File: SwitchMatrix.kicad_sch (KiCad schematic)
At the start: 0 parts

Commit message: Some matrix stuff
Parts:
- added D1, D? (x14): 1N4148, symbol Device:D_Small
- added SW1, SW? (x13): 1u, marbastlib-mx:SW_MX_1u, symbol marbastlib-mx:MX_SW_solder
- added SW?: 2u, marbastlib-mx:SW_MX_1u, symbol marbastlib-mx:MX_SW_solder
- added SW?: RotaryEncoder_Switch, symbol Device:RotaryEncoder_Switch

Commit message: Some stuff
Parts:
- removed D?: 1N4148, symbol Device:D_Small
- removed SW?: 2u, marbastlib-mx:SW_MX_1u, symbol marbastlib-mx:MX_SW_solder
- added D15, D16, D18, D20, D21, D22, D23, D24, D25, D26, D27, D28, D29, D30: 1N4148, symbol Device:D_Small
- added SW? (x13): 1u, marbastlib-mx:SW_MX_1u, symbol marbastlib-mx:MX_SW_solder
- added SW?: 1.5u, marbastlib-mx:SW_MX_1u, symbol marbastlib-mx:MX_SW_solder
- SW14: renamed from SW?; value 1u -> 2u
- gave numbers to parts that had none: 25
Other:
- moved on the sheet: SW?

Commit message: Some matrix work
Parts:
- removed D1, D10, D11, D12, D13, D14, D15, D16, D18, D2, D20, D21, D22, D23, D24, D25, D26, D27, D28, D29, D3, D30, D4, D5, D6, D7, D8, D9: 1N4148, symbol Device:D_Small
- removed SW1, SW10, SW11, SW12, SW13, SW2, SW3, SW4, SW5, SW6, SW7, SW8, SW9, SW? (x13): 1u, marbastlib-mx:SW_MX_1u, symbol marbastlib-mx:MX_SW_solder
- removed SW14: 2u, marbastlib-mx:SW_MX_1u, symbol marbastlib-mx:MX_SW_solder
- removed SW?: 1.5u, marbastlib-mx:SW_MX_1u, symbol marbastlib-mx:MX_SW_solder
- removed SW?: RotaryEncoder_Switch, symbol Device:RotaryEncoder_Switch
- added D? (x31): 1N4148, symbol Device:D_Small
- added SW? (x30): 1u, marbastlib-mx:SW_MX_1u, symbol marbastlib-mx:MX_SW_solder
- added SW?: 2u, marbastlib-mx:SW_MX_1u, symbol marbastlib-mx:MX_SW_solder
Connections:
- new net: D?.2 (A), SW?.2 (x31)

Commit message: Some more matrix stuff
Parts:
- removed D?: 1N4148, symbol Device:D_Small
- added D? (x41): 1N4148, symbol Device:D_Small
- added SW? (x34): 1u, marbastlib-mx:SW_MX_1u, symbol marbastlib-mx:MX_SW_solder
- added SW?: 7u, marbastlib-mx:SW_MX_1u, symbol marbastlib-mx:MX_SW_solder
- added SW?: 1.75u, marbastlib-mx:SW_MX_1u, symbol marbastlib-mx:MX_SW_solder
- added SW?: 2.25u, marbastlib-mx:SW_MX_1u, symbol marbastlib-mx:MX_SW_solder
- added SW? (x2): 1.5u, marbastlib-mx:SW_MX_1u, symbol marbastlib-mx:MX_SW_solder
- added SW? (x2): 1.25u, marbastlib-mx:SW_MX_1u, symbol marbastlib-mx:MX_SW_solder
- SW?: value 1u -> 1.5u
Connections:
- net COL0: now reaches SW?.1
- net COL0: now also SW?.1, SW?.1, SW?.1, SW?.1, SW?.1
- new net: D?.2 (A), SW?.2 (x41)
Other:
- moved on the sheet: D?, SW?

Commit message: Columns
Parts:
- removed D?: 1N4148, symbol Device:D_Small
- added SW? (x5): 1.25u, marbastlib-mx:SW_MX_1u, symbol marbastlib-mx:MX_SW_solder
- added SW?: 6.25u, marbastlib-mx:SW_MX_1u, symbol marbastlib-mx:MX_SW_solder
- SW?: value 1u -> 1.5u
- gave numbers to parts that had none: 6
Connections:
- net COL4: now reaches SW?.1
- net COL4: now also SW5.1, SW?.1, SW?.1
- net COL8: now reaches SW?.1
- net COL8: now also SW?.1, SW?.1, SW?.1
- net COL9: now reaches SW?.1
- net COL9: now also SW?.1, SW?.1, SW?.1, SW?.1
- net COL6: now reaches SW?.1
- net COL6: now also SW?.1, SW?.1, SW?.1, SW?.1, SW?.1
- net COL13: now reaches SW?.1
- net COL13: now also SW?.1, SW?.1, SW?.1, SW?.1
- net COL15: now reaches SW?.1
- net COL15: now also SW?.1, SW?.1, SW?.1, SW?.1
- net COL12: now reaches SW?.1
- net COL12: now also SW?.1, SW?.1, SW?.1, SW?.1
- net COL3: now reaches SW?.1
- net COL3: now also SW4.1, SW?.1, SW?.1
- net COL10: now reaches SW?.1
- net COL10: now also SW?.1, SW?.1, SW?.1
- net COL1: now reaches SW?.1
- net COL1: now also SW2.1, SW?.1, SW?.1, SW?.1, SW?.1
- net COL11: now reaches SW?.1
- net COL11: now also SW?.1, SW?.1, SW?.1, SW?.1, SW?.1
- net COL5: now reaches SW?.1
- net COL5: now also SW6.1, SW?.1, SW?.1
- net COL14: now reaches SW?.1
- net COL14: now also SW?.1
- net at D?.2 (A), SW?.2: now also SW?.2
- net COL2: now reaches SW?.1
- net COL2: now also SW3.1, SW?.1, SW?.1, SW?.1, SW?.1
- net COL7: now reaches SW?.1
- net COL7: now also SW?.1, SW?.1, SW?.1
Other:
- moved on the sheet: D?, SW?

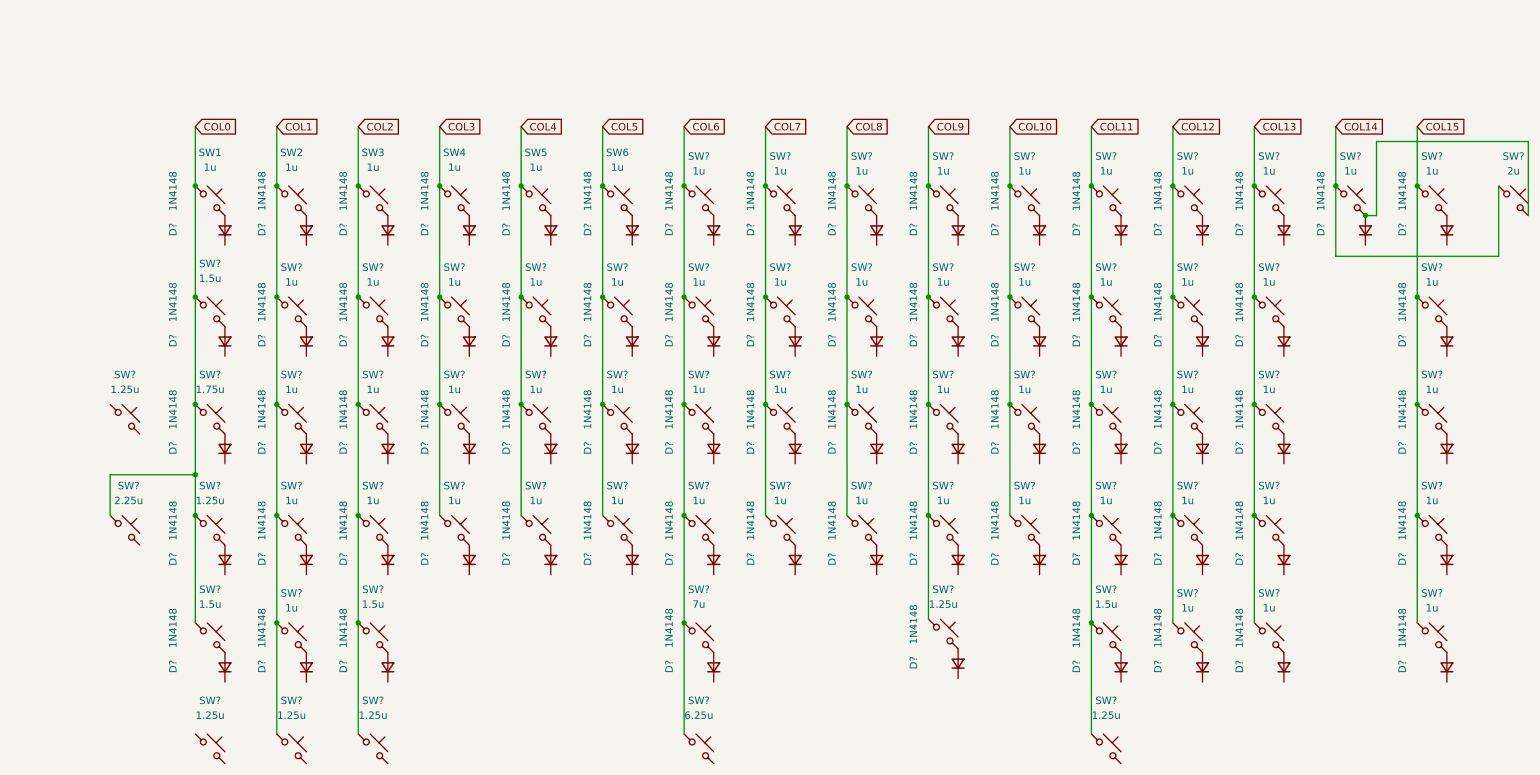
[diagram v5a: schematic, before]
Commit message: ISO + some wiring
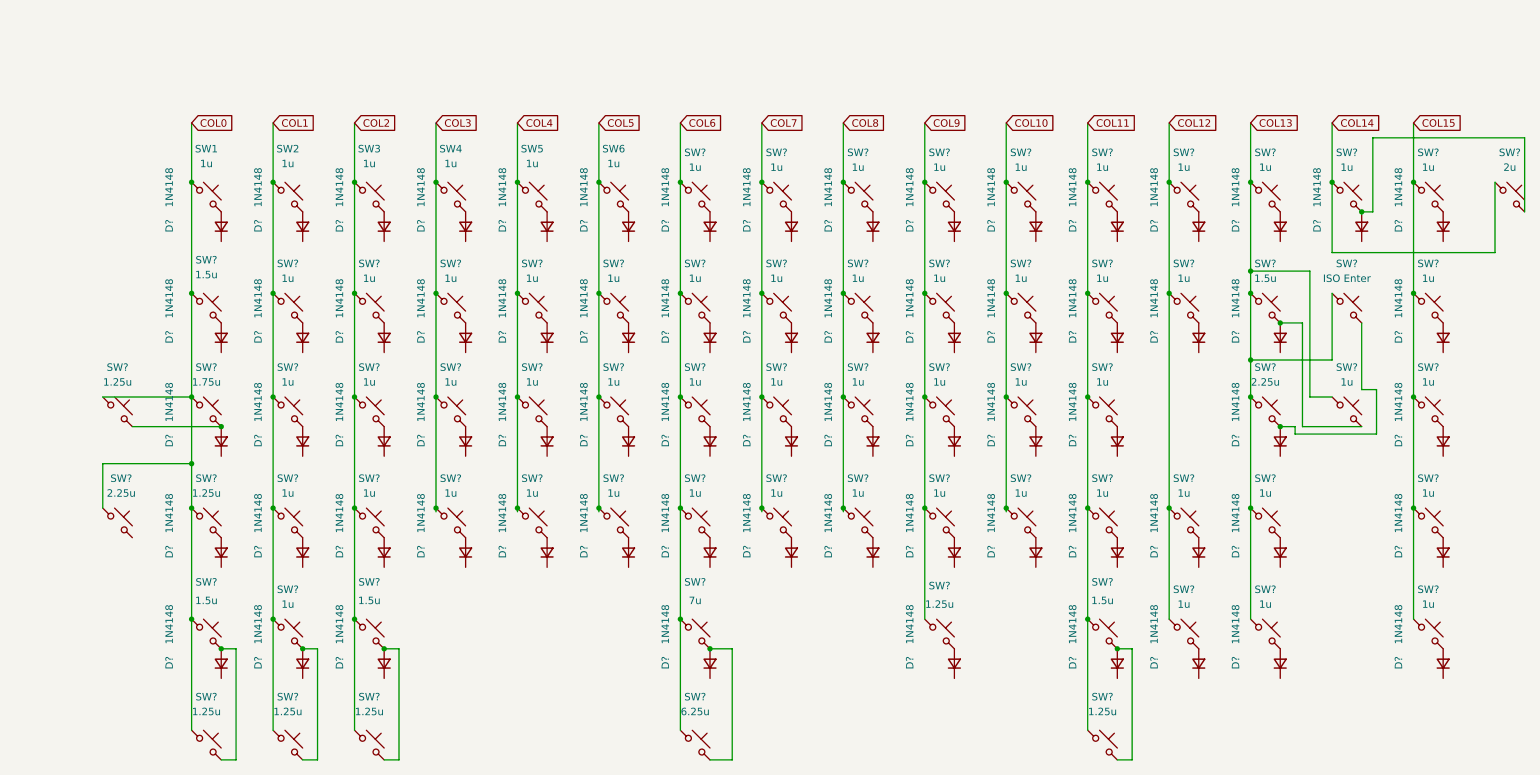
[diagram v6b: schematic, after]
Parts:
- removed D?: 1N4148, symbol Device:D_Small
- removed SW?: 1u, marbastlib-mx:SW_MX_1u, symbol marbastlib-mx:MX_SW_solder
- added SW?: ISO Enter, marbastlib-mx:SW_MX_1u, symbol marbastlib-mx:MX_SW_solder
- added SW?: 1u, marbastlib-mx:SW_MX_1u, symbol marbastlib-mx:MX_SW_solder
- SW?: value 1u -> 2.25u
- SW?: value 1u -> 1.5u
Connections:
- net COL0: now also SW?.1, SW?.1
- net COL13: now also SW?.1, SW?.1
- net at D?.2 (A), SW?.2: now also SW?.2 (x8)
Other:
- moved on the sheet: D?, SW1, SW2, SW3, SW4, SW5, SW6, SW?

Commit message: Rows
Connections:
- net ROW0: now reaches D?.1 (K)
- net ROW0: now also D?.1 (K), D?.1 (K), D?.1 (K), D?.1 (K), D?.1 (K), D?.1 (K), D?.1 (K), D?.1 (K), D?.1 (K), D?.1 (K), D?.1 (K), D?.1 (K), D?.1 (K), D?.1 (K), D?.1 (K)
- net ROW4: now reaches D?.1 (K)
- net ROW4: now also D?.1 (K), D?.1 (K), D?.1 (K), D?.1 (K), D?.1 (K), D?.1 (K), D?.1 (K), D?.1 (K)
- net ROW1: now reaches D?.1 (K)
- net ROW1: now also D?.1 (K), D?.1 (K), D?.1 (K), D?.1 (K), D?.1 (K), D?.1 (K), D?.1 (K), D?.1 (K), D?.1 (K), D?.1 (K), D?.1 (K), D?.1 (K), D?.1 (K), D?.1 (K)
- net ROW3: now reaches D?.1 (K)
- net ROW3: now also D?.1 (K), D?.1 (K), D?.1 (K), D?.1 (K), D?.1 (K), D?.1 (K), D?.1 (K), D?.1 (K), D?.1 (K), D?.1 (K), D?.1 (K), D?.1 (K), D?.1 (K), D?.1 (K)
- net at SW?.2: now also D?.2 (A), SW?.2
- net ROW2: now reaches D?.1 (K)
- net ROW2: now also D?.1 (K), D?.1 (K), D?.1 (K), D?.1 (K), D?.1 (K), D?.1 (K), D?.1 (K), D?.1 (K), D?.1 (K), D?.1 (K), D?.1 (K), D?.1 (K), D?.1 (K)

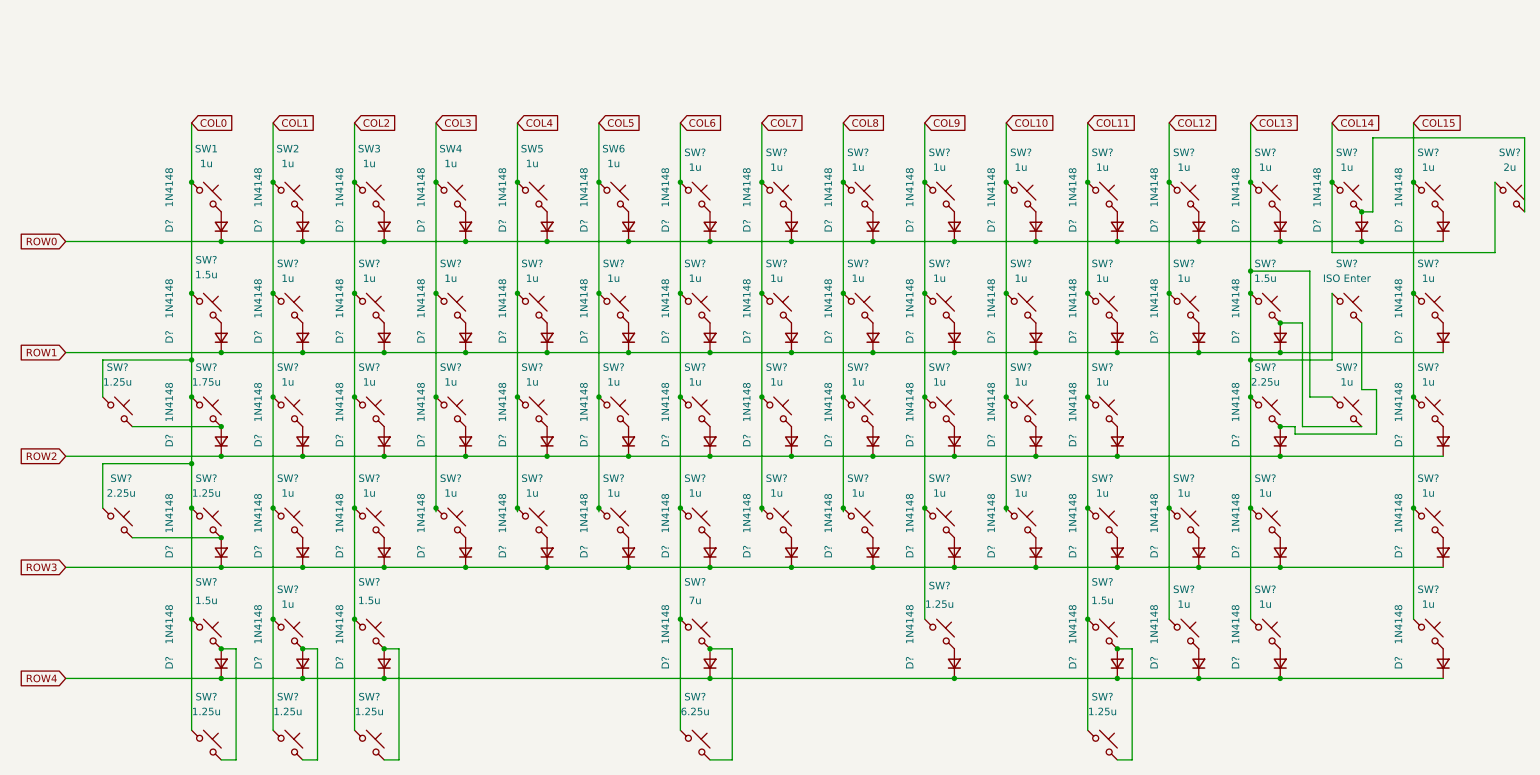
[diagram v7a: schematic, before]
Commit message: Label switches and diodes
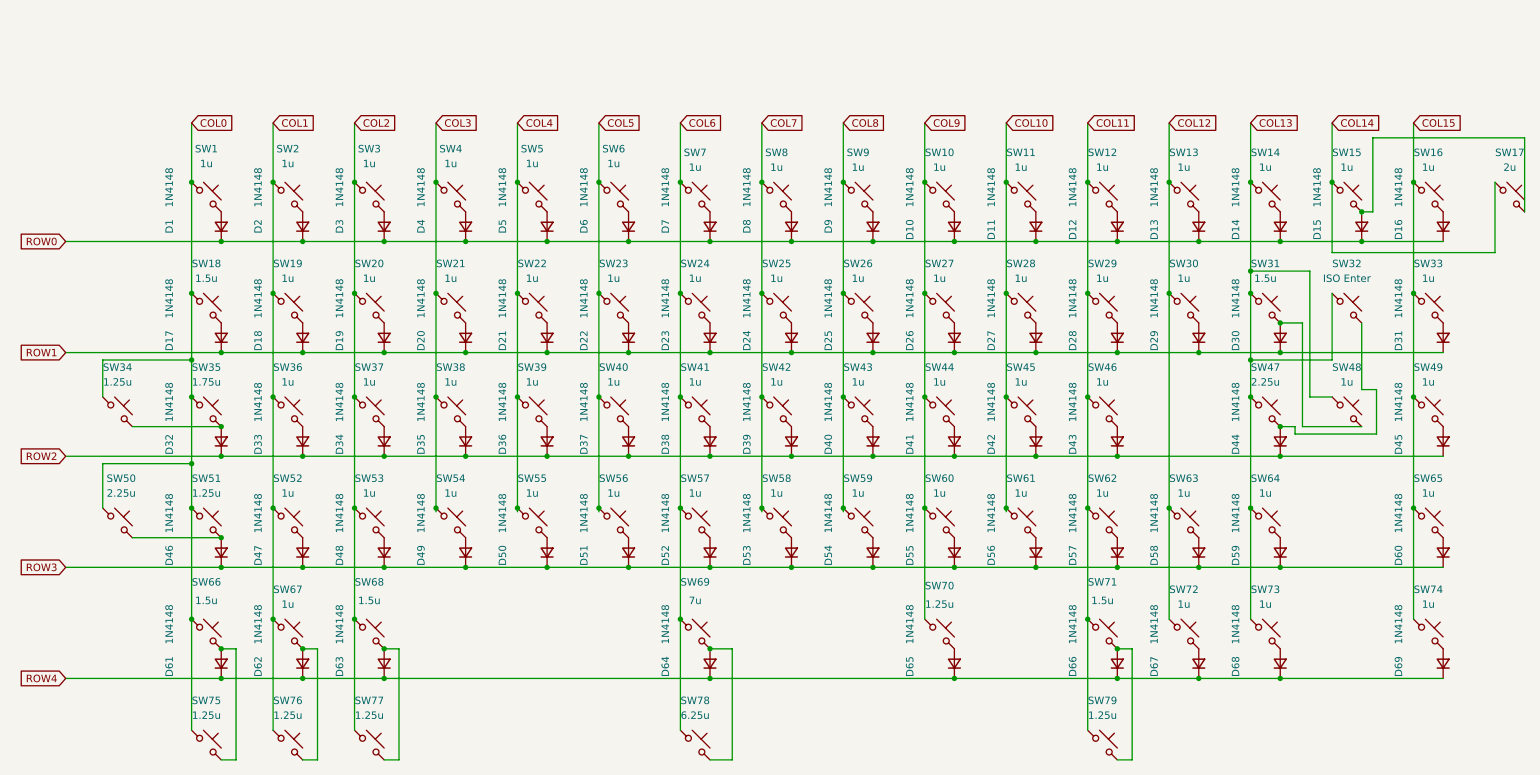
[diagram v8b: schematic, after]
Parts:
- gave numbers to parts that had none: 142
